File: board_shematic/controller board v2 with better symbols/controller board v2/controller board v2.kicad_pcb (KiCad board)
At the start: 2 copper layers, 130 x 69 mm, 22 parts, among them J1 Conn_01x03_Pin, J4 Conn_01x05_Pin, J5 Conn_01x03_Pin, J6 Conn_01x03_Pin, SW1 SW_Push, SW2 SW_Push, SW3 SW_Push, SW4 SW_Push, SW5 SW_Push, SW6 SW_Push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

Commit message: work on ensuring board is made correctly
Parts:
- removed J6: Conn_01x03_Pin, Connector_PinHeader_2.54mm:PinHeader_1x03_P2.54mm_Vertical
- added J2: Conn_01x03_Pin, Connector_PinHeader_2.54mm:PinHeader_1x03_P2.54mm_Vertical, F.Cu at (116.4, 60.0)
- added J3: Conn_01x03_Pin, Connector_PinHeader_2.54mm:PinHeader_1x03_P2.54mm_Vertical, F.Cu at (168.9, 60.0)
- A1: value Adafruit_Feather_Generic -> Adafruit_Feather_RP2040
- J4: footprint Connector_PinHeader_2.54mm:PinHeader_1x05_P2.54mm_Vertical -> Connector_PinHeader_2.54mm:PinHeader_1x05_P2.54mm_Horizontal; moved to B.Cu
- J5: value Conn_01x03_Pin -> Conn_01x07_Pin; footprint Connector_PinHeader_2.54mm:PinHeader_1x03_P2.54mm_Vertical -> Connector_PinHeader_2.54mm:PinHeader_1x07_P2.54mm_Horizontal; moved to B.Cu
- moved J5 57.7 mm to (140.0, 110.5), turned to -90 degrees
- moved SW1 52.1 mm to (129.0, 113.2)
- moved SW2 45.7 mm to (115.5, 113.2)
- moved SW5 42.4 mm to (160.8, 105.2)
- moved SW6 40.6 mm to (170.5, 95.0)
- moved J1 37.7 mm to (85.0, 94.4), turned to 0 degrees
- moved C2 16.4 mm to (176.0, 86.5)
- moved SW4 14.1 mm to (180.2, 105.2)
- moved C4 8.65 mm to (99.0, 93.0)
- moved C3 5.61 mm to (91.0, 91.5)
- moved C1 4.57 mm to (166.5, 86.5)
- moved U2 4.50 mm to (98.5, 75.0)
- moved U1 4.00 mm to (192.0, 75.0)
- moved J4 2.06 mm to (116.4, 92.0), turned to -90 degrees
- moved A1 0.14 mm to (134.7, 60.3)
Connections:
- A1 pad 10: unconnected-(A1-A5-Pad10) -> Net-(A1-D25)
- A1 pad 15: unconnected-(A1-TX-Pad15) -> Net-(A1-TX)
- A1 pad 16: Net-(A1-SPARE) -> Net-(A1-D4)
- A1 pad 17: unconnected-(A1-SDA-Pad17) -> Net-(A1-SDA)
- A1 pad 18: unconnected-(A1-SCL-Pad18) -> Net-(A1-SCL)
- A1 pad 21: Net-(A1-D2) -> Net-(A1-D9)
- A1 pad 22: Net-(A1-D3) -> Net-(A1-D10)
- A1 pad 23: Net-(A1-D4) -> Net-(A1-D11)
- A1 pad 24: Net-(A1-D5) (its old number) -> Net-(A1-D12)
- A1 pad 25: Net-(A1-D6) (its old number) -> Net-(A1-D13)
- A1 pad 9: unconnected-(A1-A4-Pad9) -> Net-(A1-D24)
- J4 pad 2: Net-(A1-RX) -> Net-(A1-D24)
- J4 pad 3: unconnected-(J4-Pin_3-Pad3) -> GND
- J4 pad 4: Net-(A1-MISO) -> Net-(A1-D25)
- J4 pad 5: +3.3V -> unconnected-(J4-Pin_5-Pad5)
- J5 pad 1: Net-(A1-D2) -> Net-(A1-D13)
- J5 pad 2: Net-(A1-D3) -> Net-(A1-SCK)
- J5 pad 3: GND -> Net-(A1-MOSI)
- SW1 pad 2: Net-(A1-D5) (its old number) -> Net-(A1-D11)
- SW2 pad 2: Net-(A1-D4) -> Net-(A1-D12)
- SW3 pad 2: Net-(A1-SPARE) -> Net-(A1-RX)
- SW4 pad 2: Net-(A1-D6) (its old number) -> Net-(A1-MISO)
- SW5 pad 2: Net-(A1-MOSI) -> Net-(A1-D4)
- SW6 pad 2: Net-(A1-SCK) -> Net-(A1-TX)
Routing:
- net GND: track 305.7 -> 0.00 mm
- net +3.3V: track 159.5 -> 0.00 mm
- net Net-(A1-A2): track 82.7 -> 0.00 mm
- net Net-(A1-A1): track 67.3 -> 0.00 mm
- net Net-(A1-A0): track 66.7 -> 0.00 mm
- net Net-(A1-SPARE): track 51.0 -> 0.00 mm
- net Net-(A1-D5): track 50.6 -> 0.00 mm
- net Net-(A1-D5) (its old number): track 47.1 -> 0.00 mm
- net Net-(A1-D6): track 47.1 -> 0.00 mm
- net Net-(A1-SCK): track 40.6 -> 0.00 mm
- net Net-(A1-MOSI): track 39.0 -> 0.00 mm
- net Net-(A1-D4): track 35.2 -> 0.00 mm
- net Net-(A1-D2): track 35.2 -> 0.00 mm
- net Net-(A1-D6) (its old number): track 34.4 -> 0.00 mm
- net Net-(A1-D3): track 33.7 -> 0.00 mm
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
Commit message: Updates to PCB design
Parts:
- C1, C2, C3, C4: moved to B.Cu
- moved C4 9.22 mm to (108.0, 91.0), turned to 180 degrees
- moved J4 4.98 mm to (117.4, 87.1)
- moved C1 1.59 mm to (165.0, 86.5), turned to 180 degrees
- moved C3 1.35 mm to (92.0, 92.5), turned to 180 degrees
- turned C2 to 180 degrees
- renumbered G*** to G34, G*** to G36, G*** to G45, REF** to REF15, REF** to REF30
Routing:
- net GND: track 0.00 -> 342.5 mm
- net +3.3V: track 0.00 -> 218.3 mm
- net Net-(A1-A0): track 0.00 -> 70.7 mm
- net Net-(A1-RX): track 0.00 -> 66.6 mm
- net Net-(A1-A2): track 0.00 -> 65.9 mm
- net Net-(A1-D12): track 0.00 -> 64.3 mm, vias 0 -> 1
- net Net-(A1-A1): track 0.00 -> 63.5 mm
- net Net-(A1-MISO): track 0.00 -> 61.5 mm
- net Net-(A1-A3): track 0.00 -> 57.5 mm
- net Net-(A1-D10): track 0.00 -> 50.8 mm
- net Net-(A1-D11): track 0.00 -> 50.1 mm, vias 0 -> 1
- net Net-(A1-D9): track 0.00 -> 47.8 mm, vias 0 -> 1
- net Net-(A1-TX): track 0.00 -> 43.8 mm
- net Net-(A1-D5): track 0.00 -> 41.8 mm
- net Net-(A1-D6): track 0.00 -> 38.7 mm
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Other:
- board text added: "This board was designed by Keith Matthews as a learning tool. It was also designed as a highly customizable gamepad controller. The inteded use is mostly as a learning device I do also plan on using this to drive a VideoRay Pro4"
- board text removed: "This board was designed by Keith Matthews as a learning tool. It was also designed as a highly customizable gamepad controller. The inteded use is mostly as a learning device I do also plan on using this to drive a VideoRay Pro4 This is what happens when you dont allow for easy customization of inputs"

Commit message: added credits file, added 3d model for 10k pot
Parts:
- U1, U2: footprint SparkFun-Electromechanical:XDCR_COM-09032 -> joystick:XDCR_COM-09032
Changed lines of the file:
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@@
     )
   )
-  (footprint "SparkFun-Electromechanical:XDCR_COM-09032" (layer "F.Cu")
+  (footprint "joystick:XDCR_COM-09032" (layer "F.Cu")
     (at 192 75)
     (property "Sheetfile" "controller board v2.kicad_sch")
@@
     )
   )
-  (footprint "SparkFun-Electromechanical:XDCR_COM-09032" (layer "F.Cu")
+  (footprint "joystick:XDCR_COM-09032" (layer "F.Cu")
     (at 98.5 75)
     (property "Sheetfile" "controller board v2.kicad_sch")

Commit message: changed hole locations, updated pin orientation
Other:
- outline, holes or cut-outs redrawn
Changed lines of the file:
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@@
   (gr_line (start 80 120) (end 80 56)
     (stroke (width 0.1) (type default)) (layer "Edge.Cuts"))
-  (gr_circle (center 85 57) (end 86.5 57)
+  (gr_circle (center 85 66) (end 86.5 66)
     (stroke (width 0.1) (type default)) (fill none) (layer "Edge.Cuts"))
   (gr_line (start 105 53.5) (end 184 53.5)
     (stroke (width 0.1) (type default)) (layer "Edge.Cuts"))
-  (gr_circle (center 205 57) (end 206.5 57)
+  (gr_circle (center 205 65.5) (end 206.5 65.5)
     (stroke (width 0.1) (type default)) (fill none) (layer "Edge.Cuts"))
   (gr_circle (center 103.5 106) (end 111.8 106)
@@
   (gr_rect (start 163.71 96.99) (end 183.71 116.99)
     (stroke (width 0.15) (type default)) (fill none) (layer "User.1"))
-  (gr_rect (start 85 57) (end 205 117)
+  (gr_rect (start 85 66) (end 205 117.5)
     (stroke (width 0.15) (type default)) (fill none) (layer "User.1"))
   (gr_line (start 80 75) (end 210 75)
@@
   )
   (dimension (type aligned) (layer "User.1")
-    (pts (xy 85 117) (xy 85 57))
+    (pts (xy 85 117) (xy 85 66))
     (height -25)
-    (gr_text "60.0000 mm" (at 58.85 87 90) (layer "User.1")
+    (gr_text "51.0000 mm" (at 58.85 91.5 90) (layer "User.1")
       (effects (font (size 1 1) (thickness 0.15)))
     )

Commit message: minor edits to pcb, end of night
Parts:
- moved A1 1.87 mm to (135.0, 58.5)
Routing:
- net GND: track 342.5 -> 0.00 mm
- net +3.3V: track 218.3 -> 0.00 mm
- net Net-(A1-A0): track 70.7 -> 0.00 mm
- net Net-(A1-RX): track 66.6 -> 0.00 mm
- net Net-(A1-A2): track 65.9 -> 0.00 mm, vias 0 -> 1
- net Net-(A1-D12): track 64.3 -> 0.00 mm
- net Net-(A1-A1): track 63.5 -> 0.00 mm
- net Net-(A1-MISO): track 61.5 -> 0.00 mm, vias 0 -> 1
- net Net-(A1-A3): track 57.5 -> 0.00 mm
- net Net-(A1-D10): track 50.8 -> 0.00 mm
- net Net-(A1-D11): track 50.1 -> 0.00 mm, vias 1 -> 2
- net Net-(A1-D9): track 47.8 -> 0.00 mm
- net Net-(A1-TX): track 43.8 -> 0.00 mm
- net Net-(A1-D5): track 41.8 -> 0.00 mm
- net Net-(A1-D6): track 38.7 -> 0.00 mm
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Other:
- outline, holes or cut-outs redrawn

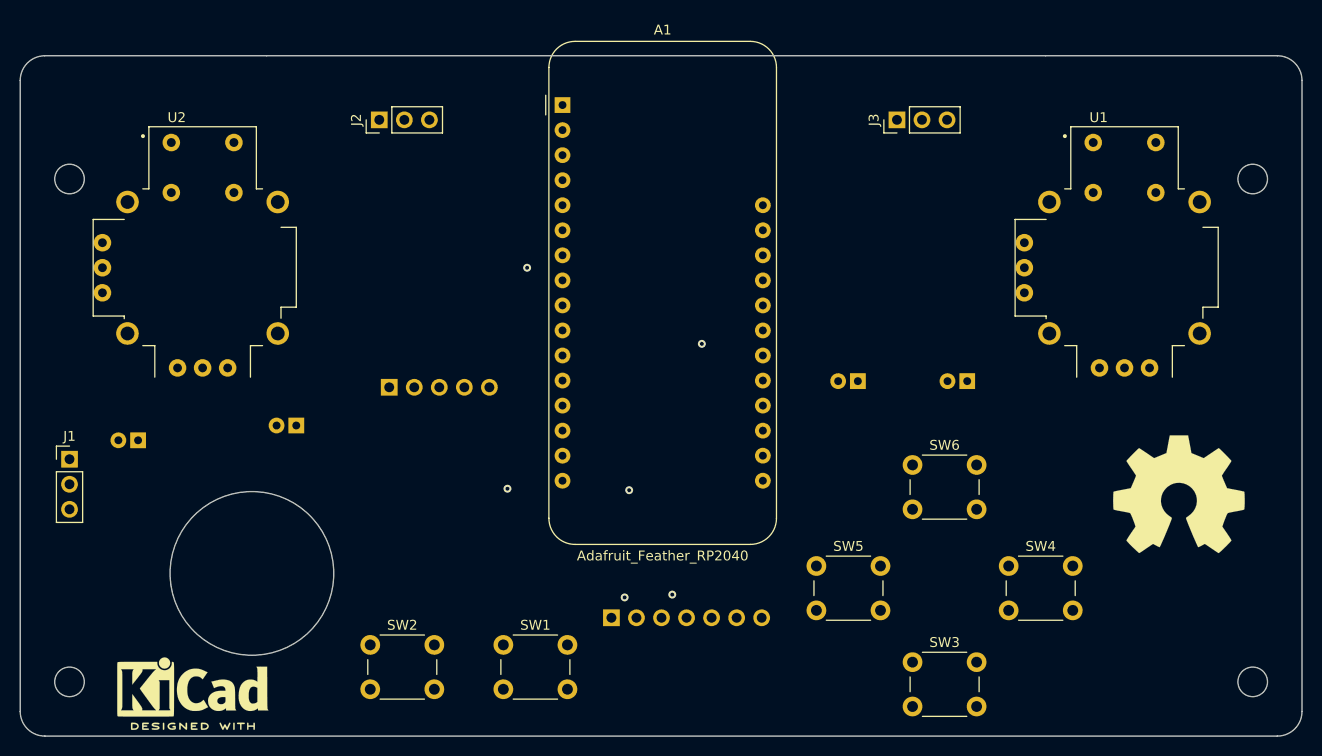
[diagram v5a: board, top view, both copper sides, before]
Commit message: updated folder structure, removed un-needed stuff
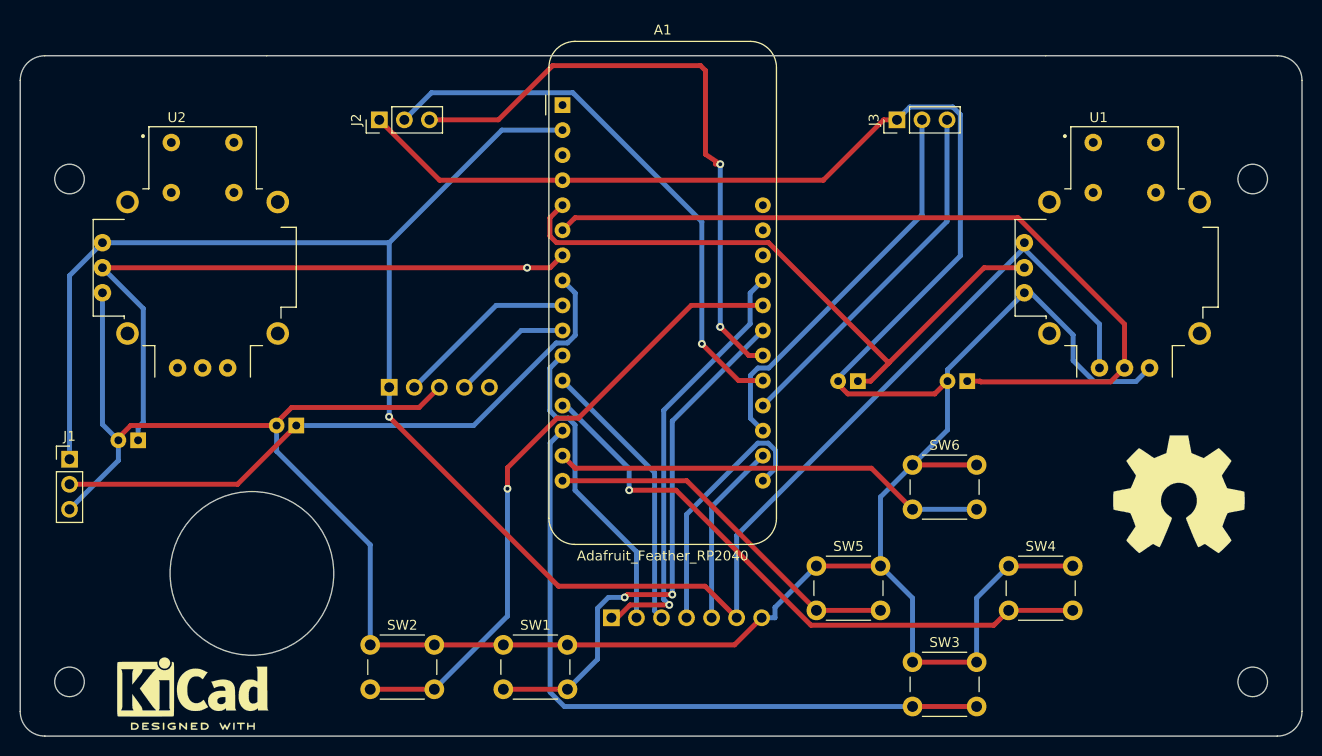
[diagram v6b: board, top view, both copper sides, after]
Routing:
- net GND: track 0.00 -> 345.0 mm
- net +3.3V: track 0.00 -> 201.5 mm, vias 0 -> 1
- net Net-(A1-A1): track 0.00 -> 83.0 mm
- net Net-(A1-RX): track 0.00 -> 70.9 mm
- net Net-(A1-A2): track 0.00 -> 66.6 mm
- net Net-(A1-A0): track 0.00 -> 65.0 mm
- net Net-(A1-D12): track 0.00 -> 64.8 mm
- net Net-(A1-D10): track 0.00 -> 63.7 mm, vias 0 -> 2
- net Net-(A1-A3): track 0.00 -> 63.7 mm
- net Net-(A1-MISO): track 0.00 -> 62.9 mm
- net Net-(A1-D9): track 0.00 -> 56.8 mm
- net Net-(A1-D11): track 0.00 -> 54.7 mm
- net Net-(A1-TX): track 0.00 -> 44.3 mm
- net Net-(A1-D13): track 0.00 -> 43.7 mm, vias 0 -> 1
- net Net-(A1-D5): track 0.00 -> 39.9 mm
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
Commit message: added images and 3d model revisions
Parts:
- moved G45 3.54 mm to (90.5, 104.0)
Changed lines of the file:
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@@
   )
   (footprint "symbols:Wojack2" (layer "B.Cu")
-    (at 90 100.5 180)
+    (at 90.5 104 180)
     (attr board_only exclude_from_pos_files exclude_from_bom)
     (fp_text reference "G45" (at 0 0) (layer "B.SilkS") hide
